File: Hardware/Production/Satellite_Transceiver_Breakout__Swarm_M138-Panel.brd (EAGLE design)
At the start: 163.8 x 103.1 mm, 386 parts, among them Q11 20V/4.2A/52mΩ/1.4W, Q13 20V/4.2A/52mΩ/1.4W, Q15 20V/4.2A/52mΩ/1.4W, Q2 20V/4.2A/52mΩ/1.4W, Q4 20V/4.2A/52mΩ/1.4W, Q5 20V/4.2A/52mΩ/1.4W, Q7 20V/4.2A/52mΩ/1.4W, Q9 20V/4.2A/52mΩ/1.4W, U1 CH340E_MSOP10, U10 CH340E_MSOP10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

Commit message: Replace 3.3V Reg with AP2112K
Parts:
- U12, U3, U6, U9: value STLQ015-3.3V -> 3.3V
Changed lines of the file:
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@@
 <attribute name="VALUE" x="17.78" y="25.781" size="0.762" layer="27" align="center"/>
 </element>
-<element name="U3" library="SparkFun-IC-Power" package="SOT23-5" value="STLQ015-3.3V" x="5.08" y="8.255" smashed="yes" rot="R90">
+<element name="U3" library="SparkFun-IC-Power" package="SOT23-5" value="3.3V" x="5.08" y="8.255" smashed="yes" rot="R90">
 <attribute name="NAME" x="2.921" y="6.477" size="0.6096" layer="25" ratio="20" rot="R90"/>
-<attribute name="PROD_ID" value="IC-15779" x="5.08" y="8.255" size="1.778" layer="27" ratio="15" rot="R90" display="off"/>
-<attribute name="VALUE" x="7.874" y="6.477" size="0.6096" layer="27" ratio="20" rot="R90"/>
+<attribute name="PROD_ID" value="VREG-12457" x="5.08" y="8.255" size="1.778" layer="27" ratio="15" rot="R90" display="off"/>
+<attribute name="VALUE" value="3.3V" x="7.874" y="6.477" size="0.6096" layer="27" ratio="20" rot="R90"/>
 </element>
 <element name="C8" library="SparkFun-Capacitors" package="0603" value="1.0uF" x="1.905" y="8.255" smashed="yes" rot="R90">
@@
 <attribute name="VALUE" x="53.848" y="25.781" size="0.762" layer="27" align="center"/>
 </element>
-<element name="U6" library="SparkFun-IC-Power" package="SOT23-5" value="STLQ015-3.3V" x="41.148" y="8.255" smashed="yes" rot="R90">
+<element name="U6" library="SparkFun-IC-Power" package="SOT23-5" value="3.3V" x="41.148" y="8.255" smashed="yes" rot="R90">
 <attribute name="NAME" x="38.989" y="6.477" size="0.6096" layer="25" ratio="20" rot="R90"/>
-<attribute name="PROD_ID" value="IC-15779" x="41.148" y="8.255" size="1.778" layer="27" ratio="15" rot="R90" display="off"/>
-<attribute name="VALUE" x="43.942" y="6.477" size="0.6096" layer="27" ratio="20" rot="R90"/>
+<attribute name="PROD_ID" value="VREG-12457" x="41.148" y="8.255" size="1.778" layer="27" ratio="15" rot="R90" display="off"/>
+<attribute name="VALUE" value="3.3V" x="43.942" y="6.477" size="0.6096" layer="27" ratio="20" rot="R90"/>
 </element>
 <element name="C20" library="SparkFun-Capacitors" package="0603" value="1.0uF" x="37.973" y="8.255" smashed="yes" rot="R90">
@@
 <attribute name="VALUE" x="89.916" y="25.781" size="0.762" layer="27" align="center"/>
 </element>
-<element name="U9" library="SparkFun-IC-Power" package="SOT23-5" value="STLQ015-3.3V" x="77.216" y="8.255" smashed="yes" rot="R90">
+<element name="U9" library="SparkFun-IC-Power" package="SOT23-5" value="3.3V" x="77.216" y="8.255" smashed="yes" rot="R90">
 <attribute name="NAME" x="75.057" y="6.477" size="0.6096" layer="25" ratio="20" rot="R90"/>
-<attribute name="PROD_ID" value="IC-15779" x="77.216" y="8.255" size="1.778" layer="27" ratio="15" rot="R90" display="off"/>
-<attribute name="VALUE" x="80.01" y="6.477" size="0.6096" layer="27" ratio="20" rot="R90"/>
+<attribute name="PROD_ID" value="VREG-12457" x="77.216" y="8.255" size="1.778" layer="27" ratio="15" rot="R90" display="off"/>
+<attribute name="VALUE" value="3.3V" x="80.01" y="6.477" size="0.6096" layer="27" ratio="20" rot="R90"/>
 </element>
 <element name="C30" library="SparkFun-Capacitors" package="0603" value="1.0uF" x="74.041" y="8.255" smashed="yes" rot="R90">
@@
 <attribute name="VALUE" x="125.984" y="25.781" size="0.762" layer="27" align="center"/>
 </element>
-<element name="U12" library="SparkFun-IC-Power" package="SOT23-5" value="STLQ015-3.3V" x="113.284" y="8.255" smashed="yes" rot="R90">
+<element name="U12" library="SparkFun-IC-Power" package="SOT23-5" value="3.3V" x="113.284" y="8.255" smashed="yes" rot="R90">
 <attribute name="NAME" x="111.125" y="6.477" size="0.6096" layer="25" ratio="20" rot="R90"/>
-<attribute name="PROD_ID" value="IC-15779" x="113.284" y="8.255" size="1.778" layer="27" ratio="15" rot="R90" display="off"/>
-<attribute name="VALUE" x="116.078" y="6.477" size="0.6096" layer="27" ratio="20" rot="R90"/>
+<attribute name="PROD_ID" value="VREG-12457" x="113.284" y="8.255" size="1.778" layer="27" ratio="15" rot="R90" display="off"/>
+<attribute name="VALUE" value="3.3V" x="116.078" y="6.477" size="0.6096" layer="27" ratio="20" rot="R90"/>
 </element>
 <element name="C40" library="SparkFun-Capacitors" package="0603" value="1.0uF" x="110.109" y="8.255" smashed="yes" rot="R90">

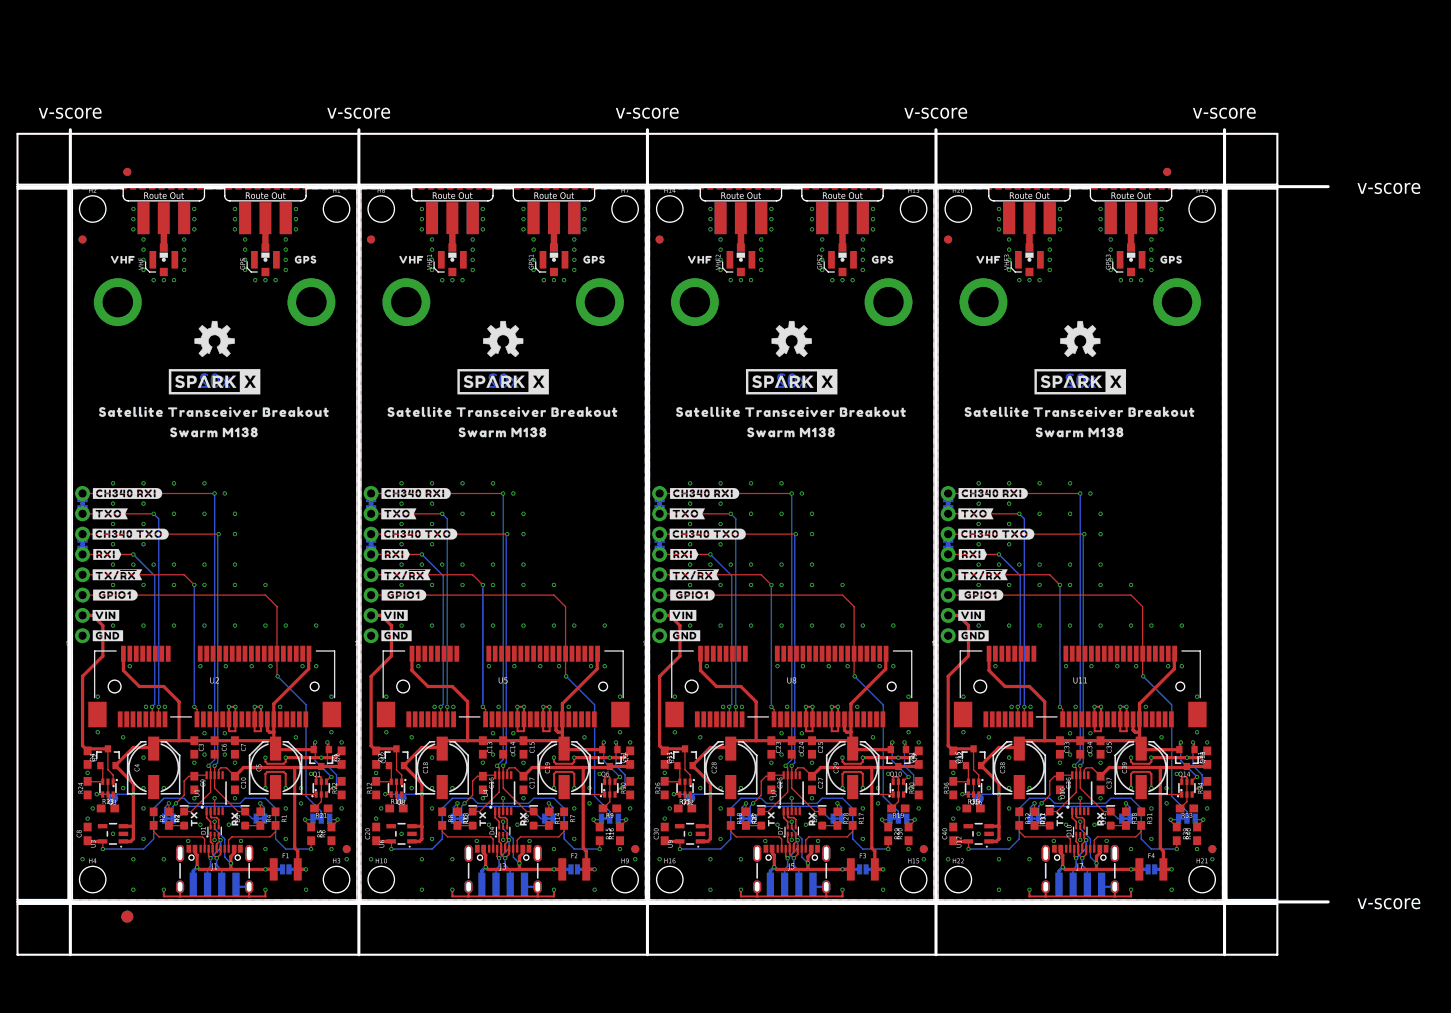
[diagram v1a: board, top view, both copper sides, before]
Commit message: Updates for x03 PCB - move standoffs by 0.6mm and add route-out gaps in panel
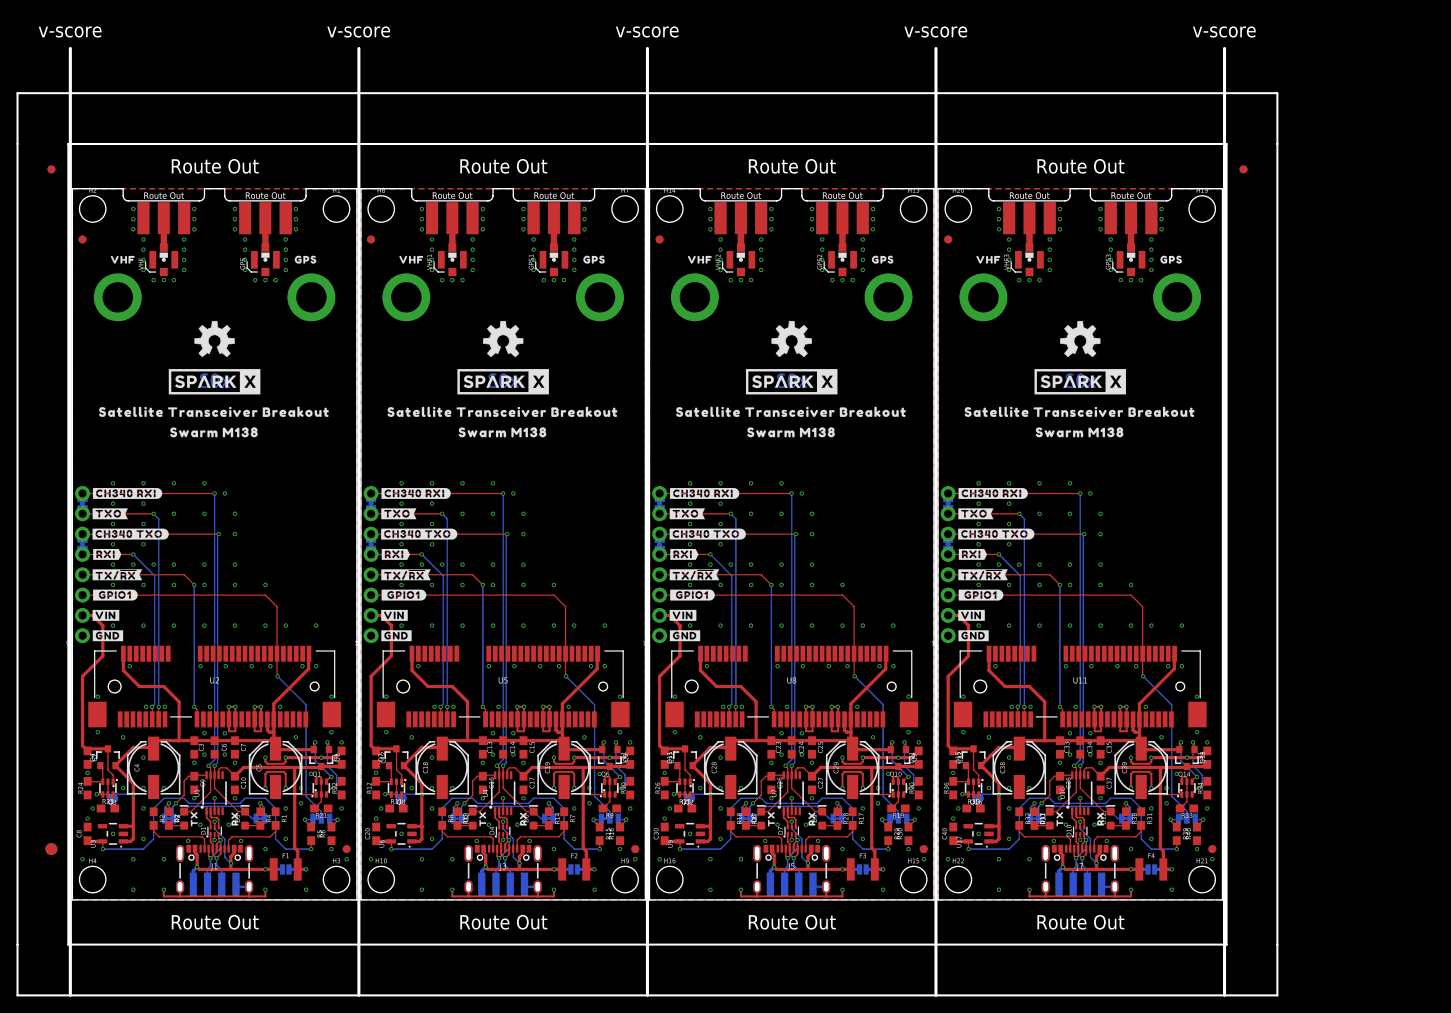
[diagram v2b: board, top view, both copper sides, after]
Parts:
- moved E$5 12.7 mm to (-2.62, 6.35)
- moved E$6 12.7 mm to (-2.62, 6.35)
- moved E$3 9.55 mm to (146.4, 91.3)
- moved E$4 9.55 mm to (146.4, 91.3)
- moved E$1 9.49 mm to (-2.62, 91.3)
- moved E$2 9.49 mm to (-2.62, 91.3)
- moved H11 0.60 mm to (41.7, 75.3)
- moved H12 0.60 mm to (65.9, 75.3)
- moved H17 0.60 mm to (77.8, 75.3)
- moved H18 0.60 mm to (102.0, 75.3)
- moved H23 0.60 mm to (113.9, 75.3)
- moved H24 0.60 mm to (138.1, 75.3)
- moved H5 0.60 mm to (5.68, 75.3)
- moved H6 0.60 mm to (29.9, 75.3)
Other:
- board size 163.8 x 103.1 mm -> 157.5 x 118.4 mm
- board text added: "x03"
- board text removed: "x02"
